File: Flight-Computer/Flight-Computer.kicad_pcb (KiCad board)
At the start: 4 copper layers, 93.7 x 43.7 mm, 124 parts, among them J1 Jumper_NO, J2 Jumper_NO, J3 Conn_01x04, J4 Conn_01x04, J5 Conn_01x04, J6 Conn_01x04, P1 647676-2, P10 Micro_SD_Card, P2 1546551-2, P3 3220-20-0200-00, P4 440054-3, P5 440054-3, P6 440054-3, P7 440054-3, P8 USB, P9 1984659, Q1 QS5U17TR, Q2 QS5U17TR, Q3 QS5U17TR, Q4 QS5U17TR, Q5 QS5U17TR, Q6 QS5U17TR, U1 STM32H750VBTx, U10 TS391IYLT, U11 TS391IYLT, U12 BMM350, U13 MIC5365-1.8YC5-TR, U2 LMS8117AMP-3.3_NOPB, U3 BMI323, U4 MAX-8C-0-10, U5 BMP390, U6 SST25VF040B-50-4I-S2AE-T, U7 RFM95W-868S2, U8 CP2102-GMR(QFN28), U9 TS391IYLT, Y1 ECS-240-18-33-JGN-TR

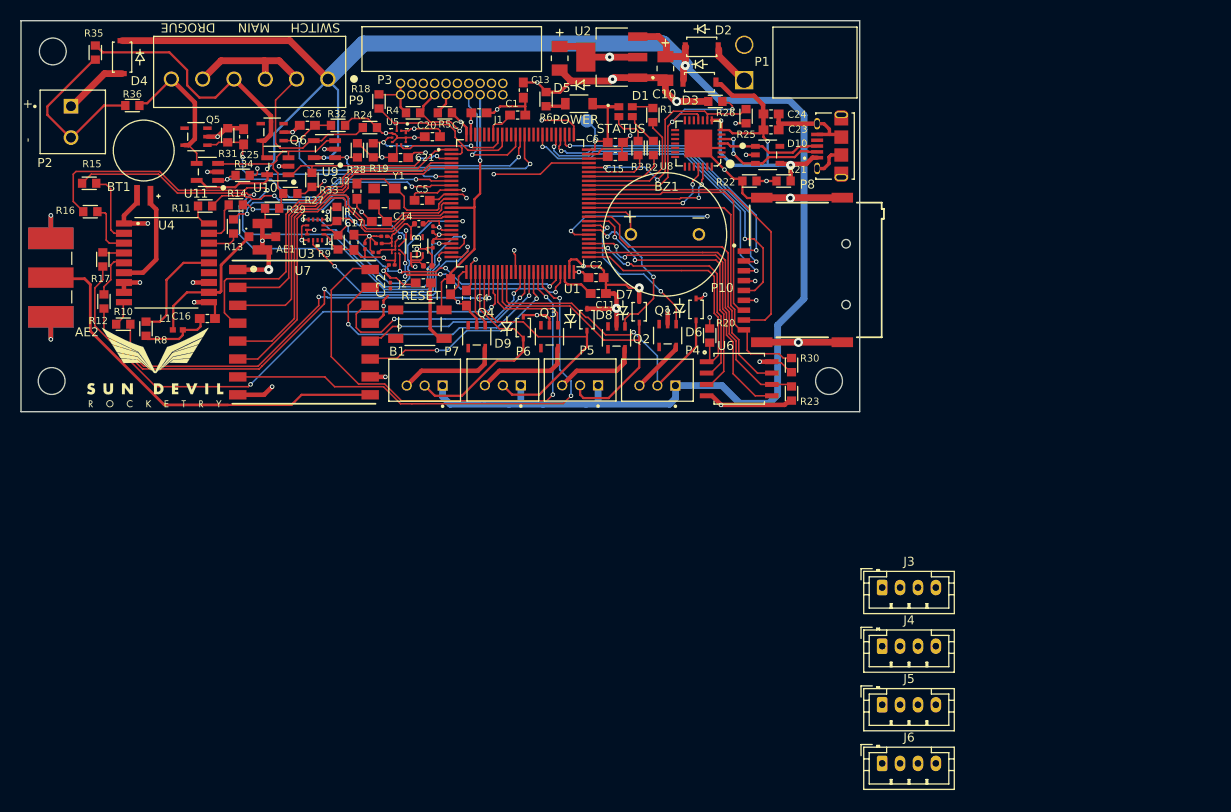
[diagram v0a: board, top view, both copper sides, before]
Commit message: Ports
Added 2 UART ports for connectivity, expanded board
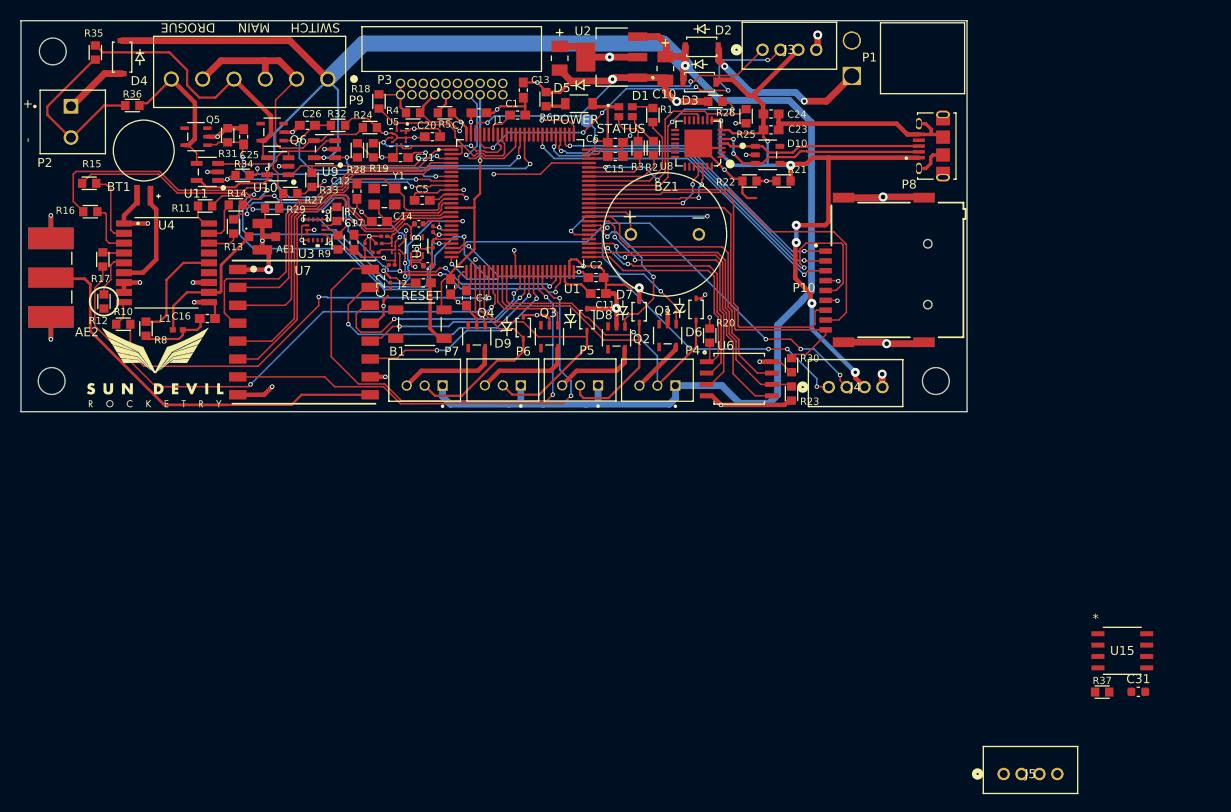
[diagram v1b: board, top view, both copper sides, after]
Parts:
- removed J6: Conn_01x04, Connector_JST:JST_PH_B4B-PH-K_1x04_P2.00mm_Vertical
- added C31: 0.1u, Capacitor_SMD:C_0603_1608Metric, F.Cu at (217.8, 132.9)
- added R37: 10k, Flight-Computer-Mac:RES_0603, F.Cu at (213.8, 132.9)
- added U15: SST25VF512A-33-4I-SAE, SST25:SOIC8_SA_SST_MCH, F.Cu at (216.0, 128.3)
- J3, J4, J5: value Conn_01x04 -> 440054-4; footprint Connector_JST:JST_PH_B4B-PH-K_1x04_P2.00mm_Vertical -> 440054_4:CONN_440054-4_TEC
- moved J3 61.6 mm to (175.8, 61.1)
- moved J4 29.6 mm to (183.2, 98.8)
- moved J5 15.6 mm to (202.8, 142.1)
- moved P1 12.0 mm to (185.8, 64.1)
- moved H3 11.9 mm to (195.2, 98.2)
- moved P8 11.4 mm to (196.0, 71.9)
- moved P10 9.13 mm to (194.3, 86.2)
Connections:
- J3 pad 1: PUART_TX -> PORT1_TX
- J3 pad 2: PUART_RX -> PORT1_RX
- J4 pad 1: PUART_TX -> PORT2_TX
- J4 pad 2: PUART_RX -> PORT2_RX
- J5 pad 1: PUART_TX -> PORT3_RX
- J5 pad 2: PUART_RX -> PORT3_TX
- U1 pad 24: IMU_INT2 -> PORT2_TX
- U1 pad 25: GPS_INT -> PORT2_RX
- U1 pad 97: unconnected-(U1-PE0-Pad97) -> PORT1_RX
- U1 pad 98: unconnected-(U1-PE1-Pad98) -> PORT1_TX
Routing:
- net PORT2_RX: track 0.00 -> 64.3 mm, vias 0 -> 4
- net GPS_INT: track 56.3 -> 0.05 mm, vias 2 -> 0
- net 5V: track 38.4 -> 89.7 mm, vias 3 -> 7
- net PORT2_TX: track 0.00 -> 49.5 mm, vias 0 -> 4
- net PORT1_RX: track 0.00 -> 42.9 mm, vias 0 -> 6
- net PORT1_TX: track 0.00 -> 36.8 mm, vias 0 -> 2
- net IMU_INT2: track 21.9 -> 0.00 mm, vias 2 -> 0
- net Earth: track 240.6 -> 256.5 mm, vias 44 -> 46
- net /PIN_HARN: track 4.73 -> 19.2 mm, vias 0 -> 2
- net SD_DAT0: track 29.5 -> 42.2 mm
- net SD_CLK: track 38.3 -> 49.7 mm
- net /Peripherals/D+: track 11.4 -> 22.8 mm
- net /Peripherals/D-: track 13.4 -> 24.7 mm
- net ~{SD_DETECT}: track 37.5 -> 44.8 mm
- net SD_DAT1: track 35.4 -> 42.2 mm
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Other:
- board size 93.7 x 43.7 mm -> 105.7 x 43.7 mm

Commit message: most up to date rev 2.5 files
third connector (where micro sd used to be) does not have tx3 pins connected (pin outs needed in order to wire)
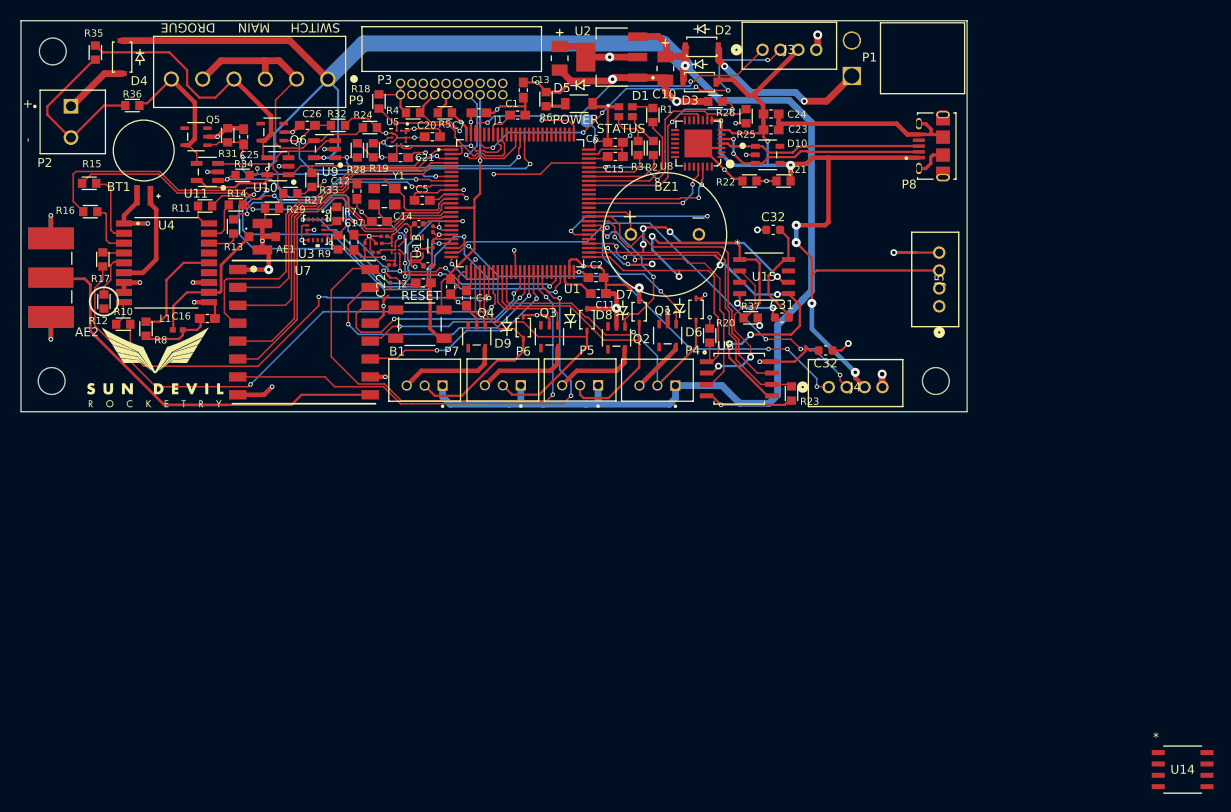
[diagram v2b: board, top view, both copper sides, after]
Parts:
- removed P10: Micro_SD_Card, Flight-Computer:MEM2075-00-140-01-A
- removed R30: 10k, Flight-Computer:RES_0603
- added C32: 0.1u, Capacitor_SMD:C_0603_1608Metric, F.Cu at (182.9, 94.8)
- added C32: 0.1u, Capacitor_SMD:C_0603_1608Metric, F.Cu at (177.0, 81.3)
- added U14: SST25VF512A-33-4I-SAE, SST25:SOIC8_SA_SST_MCH, F.Cu at (222.8, 141.6)
- C30: value 10uF -> 1uF
- moved U15 57.9 mm to (176.0, 86.5)
- moved C31 57.7 mm to (178.0, 91.1)
- moved R37 57.4 mm to (174.5, 91.1)
- moved J5 52.8 mm to (195.6, 89.8), turned to 90 degrees
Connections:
- C30 pad 1: Earth -> 1.8V
- C30 pad 2: 1.8V -> Earth
- R37 pad 1: FLASH2_SS -> ~{FLASH_SS}
- U15 pad 1: FLASH2_SS -> ~{FLASH_SS}
- U15 pad 2: FLASH2_MISO -> FLASH_MISO
- U15 pad 5: FLASH2_MOSI -> FLASH_MOSI
- U15 pad 6: FLASH2_SCK -> FLASH_SCK
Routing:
- net SD_CLK: track 49.7 -> 0.00 mm, vias 2 -> 0
- net ~{SD_DETECT}: track 44.8 -> 0.00 mm
- net SD_DAT0: track 42.2 -> 0.00 mm
- net SD_DAT1: track 42.2 -> 0.03 mm
- net SD_CMD: track 39.1 -> 0.00 mm, vias 2 -> 0
- net SD_DAT3: track 37.1 -> 0.00 mm, vias 2 -> 0
- net SD_DAT2: track 34.7 -> 0.00 mm, vias 2 -> 0
- net ~{FLASH_SS}: track 27.7 -> 55.2 mm, vias 0 -> 2
- net FLASH_SCK: track 34.2 -> 55.7 mm, vias 0 -> 4
- net 3.3V: track 97.8 -> 114.5 mm
- net 5V: track 89.7 -> 104.9 mm
- net FLASH_MOSI: track 34.3 -> 48.3 mm, vias 2 -> 6
- net Earth: track 256.5 -> 250.9 mm, vias 46 -> 48
- net ~{FLASH_HOLD}: track 34.0 -> 35.5 mm
- net FLASH_MISO: track 27.8 -> 26.5 mm, vias 2 -> 5
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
